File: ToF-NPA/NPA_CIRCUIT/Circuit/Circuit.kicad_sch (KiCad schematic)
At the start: 11 parts, among them J1 BG302-02-A-L-G

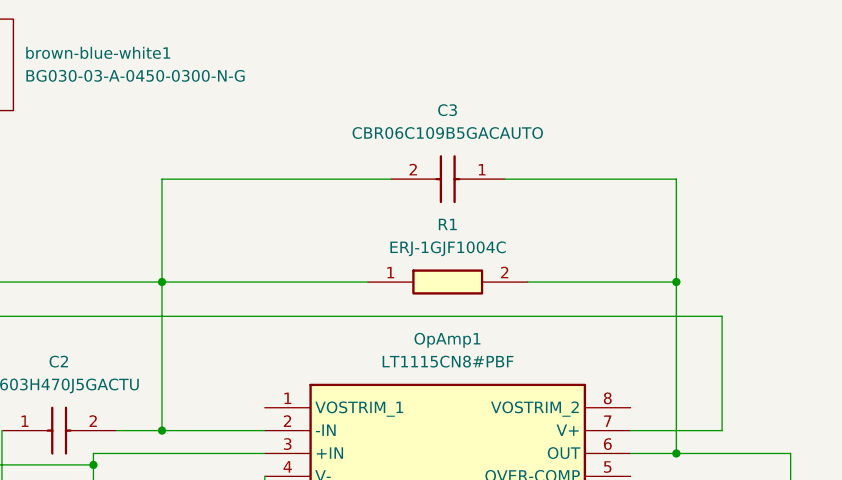
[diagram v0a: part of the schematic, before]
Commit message: changed resistor to 2W rating
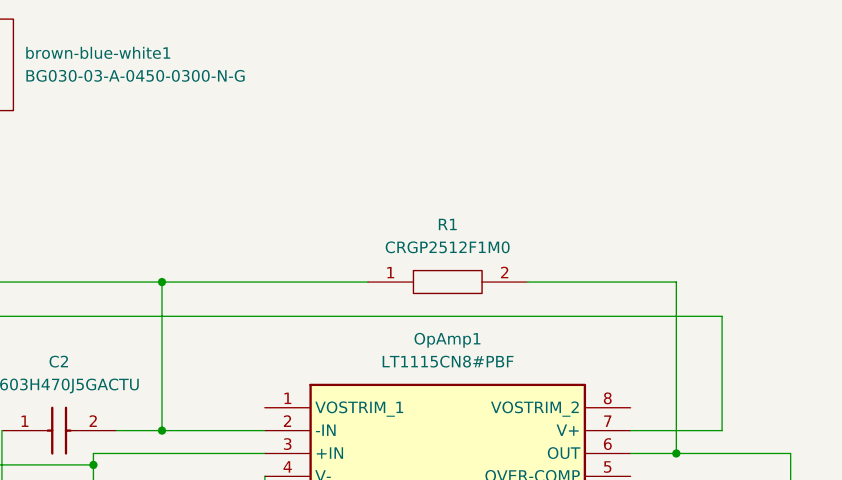
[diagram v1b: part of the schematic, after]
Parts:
- removed C3: CBR06C109B5GACAUTO, 1 pF KEMET:CBR06, symbol CBR06C109B5GACAUTO:CBR06C109B5GACAUTO
- removed R1: ERJ-1GJF1004C, 1 MOhms R:ERJ1GJJ2R4C, symbol ERJ-1GJF1004C:ERJ-1GJF1004C
- added R1: CRGP2512F1M0, RESC6432X65N, symbol CRGP2512F1M0:CRGP2512F1M0
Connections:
- net at C2.2, OpAmp1.2 (-IN), brown-blue-white1.3: now also R1.1
- net at Channel2.1, OpAmp1.6 (OUT): now also R1.2
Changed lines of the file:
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@@
-	)
-	(junction
-		(at 213.36 76.2)
-		(diameter 0)
-		(color 0 0 0 0)
 	)
 	(junction
@@
 	(wire
 		(pts
-			(xy 213.36 64.77) (xy 213.36 76.2)
-		)
-		(stroke
-			(width 0)
-			(type default)
-		)
-	)
-	(wire
-		(pts
 			(xy 113.03 96.52) (xy 113.03 101.6)
 		)
@@
 	(wire
 		(pts
-			(xy 194.31 64.77) (xy 213.36 64.77)
-		)
-		(stroke
-			(width 0)
-			(type default)
-		)
-	)
-	(wire
-		(pts
 			(xy 140.97 99.06) (xy 148.59 99.06)
 		)
@@
 	(wire
 		(pts
-			(xy 156.21 64.77) (xy 181.61 64.77)
-		)
-		(stroke
-			(width 0)
-			(type default)
-		)
-	)
-	(wire
-		(pts
 			(xy 113.03 96.52) (xy 92.71 96.52)
-		)
-		(stroke
-			(width 0)
-			(type default)
-		)
-	)
-	(wire
-		(pts
-			(xy 156.21 64.77) (xy 156.21 76.2)
 		)
 		(stroke
@@
 	)
 	(symbol
-		(lib_id "CBR06C109B5GACAUTO:CBR06C109B5GACAUTO")
-		(at 194.31 64.77 180)
-		(unit 1)
-		(exclude_from_sim no)
-		(in_bom yes)
-		(on_board yes)
-		(dnp no)
-		(fields_autoplaced yes)
-		(property "Reference" "C3"
-			(at 187.96 57.15 0)
-			(effects
-				(font
-					(size 1.27 1.27)
-				)
-			)
-		)
-		(property "Value" "CBR06C109B5GACAUTO"
-			(at 187.96 59.69 0)
-			(effects
-				(font
-					(size 1.27 1.27)
-				)
-			)
-		)
-		(property "Footprint" "1 pF KEMET:CBR06"
-			(at 185.42 -31.42 0)
-			(effects
-				(font
-					(size 1.27 1.27)
-				)
-				(justify left top)
-				(hide yes)
-			)
-		)
-		(property "Datasheet" "https://search.kemet.com/download/datasheet/CBR06C109B5GACAUTO"
-			(at 185.42 -131.42 0)
-			(effects
-				(font
-					(size 1.27 1.27)
-				)
-				(justify left top)
-				(hide yes)
-			)
-		)
-		(property "Description" "Multilayer Ceramic Capacitors MLCC - SMD/SMT 50Vol 1pF C0G 0.10pF 0603 AEC-Q200"
-			(at 194.31 64.77 0)
-			(effects
-				(font
-					(size 1.27 1.27)
-				)
-				(hide yes)
-			)
-		)
-		(property "Height" ""
-			(at 185.42 -331.42 0)
-			(effects
-				(font
-					(size 1.27 1.27)
-				)
-				(justify left top)
-				(hide yes)
-			)
-		)
-		(property "Mouser Part Number" "80-CBR06C109B5GAUTO"
-			(at 185.42 -431.42 0)
-			(effects
-				(font
-					(size 1.27 1.27)
-				)
-				(justify left top)
-				(hide yes)
-			)
-		)
-		(property "Mouser Price/Stock" "https://www.mouser.co.uk/ProductDetail/KEMET/CBR06C109B5GACAUTO?qs=By6Nw2ByBD3Q%252BDdQ3pawMw%3D%3D"
-			(at 185.42 -531.42 0)
-			(effects
-				(font
-					(size 1.27 1.27)
-				)
-				(justify left top)
-				(hide yes)
-			)
-		)
-		(property "Manufacturer_Name" "KEMET"
-			(at 185.42 -631.42 0)
-			(effects
-				(font
-					(size 1.27 1.27)
-				)
-				(justify left top)
-				(hide yes)
-			)
-		)
-		(property "Manufacturer_Part_Number" "CBR06C109B5GACAUTO"
-			(at 185.42 -731.42 0)
-			(effects
-				(font
-					(size 1.27 1.27)
-				)
-				(justify left top)
-				(hide yes)
-			)
-		)
-		(pin "1"
-		)
-		(pin "2"
-		)
-		(instances
-			(project "Circuit"
-				(path "/9da35d7f-0531-4114-9242-19da34b83f92"
-					(reference "C3")
-					(unit 1)
-				)
-			)
-		)
-	)
-	(symbol
 		(lib_id "CONBNC002:CONBNC002")
 		(at 228.6 118.11 270)
@@
 	)
 	(symbol
-		(lib_id "ERJ-1GJF1004C:ERJ-1GJF1004C")
-		(at 179.07 76.2 0)
-		(unit 1)
-		(exclude_from_sim no)
-		(in_bom yes)
-		(on_board yes)
-		(dnp no)
-		(fields_autoplaced yes)
-		(property "Reference" "R1"
-			(at 187.96 69.85 0)
-			(effects
-				(font
-					(size 1.27 1.27)
-				)
-			)
-		)
-		(property "Value" "ERJ-1GJF1004C"
-			(at 187.96 72.39 0)
-			(effects
-				(font
-					(size 1.27 1.27)
-				)
-			)
-		)
-		(property "Footprint" "1 MOhms R:ERJ1GJJ2R4C"
-			(at 193.04 172.39 0)
-			(effects
-				(font
-					(size 1.27 1.27)
-				)
-				(justify left top)
-				(hide yes)
-			)
-		)
-		(property "Datasheet" "https://industrial.panasonic.com/cdbs/www-data/pdf/RDA0000/AOA0000C304.pdf"
-			(at 193.04 272.39 0)
-			(effects
-				(font
-					(size 1.27 1.27)
-				)
-				(justify left top)
-				(hide yes)
-			)
-		)
-		(property "Description" "Series/Type: Precision Thick Film Chip Resistors, Power Rating (W): 0.05, Chip Size (LxW(EIA)) (mm): 0.6 x 0.3 (EIA:0201), Resistance Values (): 1000000, Resistance Tolerance (%): 1, T.C.R (10/K): +/-200"
-			(at 179.07 76.2 0)
-			(effects
-				(font
-					(size 1.27 1.27)
-				)
-				(hide yes)
-			)
-		)
-		(property "Height" "0.26"
-			(at 193.04 472.39 0)
-			(effects
-				(font
-					(size 1.27 1.27)
-				)
-				(justify left top)
-				(hide yes)
-			)
-		)
-		(property "Mouser Part Number" "667-ERJ-1GJF1004C"
-			(at 193.04 572.39 0)
-			(effects
-				(font
-					(size 1.27 1.27)
-				)
-				(justify left top)
-				(hide yes)
-			)
-		)
-		(property "Mouser Price/Stock" "https://www.mouser.co.uk/ProductDetail/Panasonic/ERJ-1GJF1004C?qs=OcgtsXO%252B3gt%252B%2FF8grdzXWA%3D%3D"
-			(at 193.04 672.39 0)
-			(effects
-				(font
-					(size 1.27 1.27)
-				)
-				(justify left top)
-				(hide yes)
-			)
-		)
-		(property "Manufacturer_Name" "Panasonic"
-			(at 193.04 772.39 0)
-			(effects
-				(font
-					(size 1.27 1.27)
-				)
-				(justify left top)
-				(hide yes)
-			)
-		)
-		(property "Manufacturer_Part_Number" "ERJ-1GJF1004C"
-			(at 193.04 872.39 0)
-			(effects
-				(font
-					(size 1.27 1.27)
-				)
-				(justify left top)
-				(hide yes)
-			)
-		)
-		(pin "2"
-		)
-		(pin "1"
-		)
-		(instances
-			(project "Circuit"
-				(path "/9da35d7f-0531-4114-9242-19da34b83f92"
-					(reference "R1")
-					(unit 1)
-				)
-			)
-		)
-	)
-	(symbol
 		(lib_id "LT1115CN8#PBF:LT1115CN8#PBF")
 		(at 167.64 90.17 0)
@@
 					(unit 1)
 				)
+			)
+		)
+	)
+	(symbol
+		(lib_id "CRGP2512F1M0:CRGP2512F1M0")
+		(at 179.07 76.2 0)
+		(unit 1)
+		(exclude_from_sim no)
+		(in_bom yes)
+		(on_board yes)
+		(dnp no)
+		(fields_autoplaced yes)
+		(property "Reference" "R1"
+			(at 187.96 69.85 0)
+			(effects
+				(font
+					(size 1.27 1.27)
+				)
+			)
+		)
+		(property "Value" "CRGP2512F1M0"
+			(at 187.96 72.39 0)
+			(effects
+				(font
+					(size 1.27 1.27)
+				)
+			)
+		)
+		(property "Footprint" "RESC6432X65N"
+			(at 193.04 74.93 0)
+			(effects
+				(font
+					(size 1.27 1.27)
+				)
+				(justify left)
+				(hide yes)
+			)
+		)
+		(property "Datasheet" "https://www.te.com/commerce/DocumentDelivery/DDEController?Action=srchrtrv&DocNm=9-1773463-9&DocType=DS&DocLang=English"
+			(at 193.04 77.47 0)
+			(effects
+				(font
+					(size 1.27 1.27)
+				)
+				(justify left)
+				(hide yes)
+			)
+		)
+		(property "Description" "1M 2512 Thick Film Resistor +/-1% 2W CRGP2512F1M0"
+			(at 193.04 80.01 0)
+			(effects
+				(font
+					(size 1.27 1.27)
+				)
+				(justify left)
+				(hide yes)
+			)
+		)
+		(property "Height" "0.65"
+			(at 193.04 82.55 0)
+			(effects
+				(font
+					(size 1.27 1.27)
+				)
+				(justify left)
+				(hide yes)
+			)
+		)
+		(property "Mouser Part Number" "279-CRGP2512F1M0"
+			(at 193.04 85.09 0)
+			(effects
+				(font
+					(size 1.27 1.27)
+				)
+				(justify left)
+				(hide yes)
+			)
+		)
+		(property "Mouser Price/Stock" "https://www.mouser.co.uk/ProductDetail/TE-Connectivity-Holsworthy/CRGP2512F1M0?qs=wUXugUrL1qwpbWEKgYeyog%3D%3D"
+			(at 193.04 87.63 0)
+			(effects
+				(font
+					(size 1.27 1.27)
+				)
+				(justify left)
+				(hide yes)
+			)
+		)
+		(property "Manufacturer_Name" "TE Connectivity"
+			(at 193.04 90.17 0)
+			(effects
+				(font
+					(size 1.27 1.27)
+				)
+				(justify left)
+				(hide yes)
+			)
+		)
+		(property "Manufacturer_Part_Number" "CRGP2512F1M0"
+			(at 193.04 92.71 0)
+			(effects
+				(font
+					(size 1.27 1.27)
+				)
+				(justify left)
+				(hide yes)
+			)
+		)
+		(pin "2"
+		)
+		(pin "1"
+		)
+		(instances
+			(project "Circuit"
+				(path "/9da35d7f-0531-4114-9242-19da34b83f92"
+					(reference "R1")
+					(unit 1)
+				)
